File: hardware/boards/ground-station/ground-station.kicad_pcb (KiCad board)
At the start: 4 copper layers, 65 x 59.5 mm, 122 parts, among them J1 USB_A, J101 Raspberry_Pi_2_3, J102 Conn_01x15, J2 Barrel_Jack, J201 U.FL, J202 U.FL, J203 U.FL, J3 Conn_Coaxial, U201 SX1262IMLTRT, U202 RX5808, U203 SW-GPS01, U204 SKY13453-385LF, U3 TPS564242DRLR, U601 ADV7282A-M, U602 AP2127K-1.8, U603 AP2127K-1.8, Y201 32 MHz, Y601 28.63636 MHz

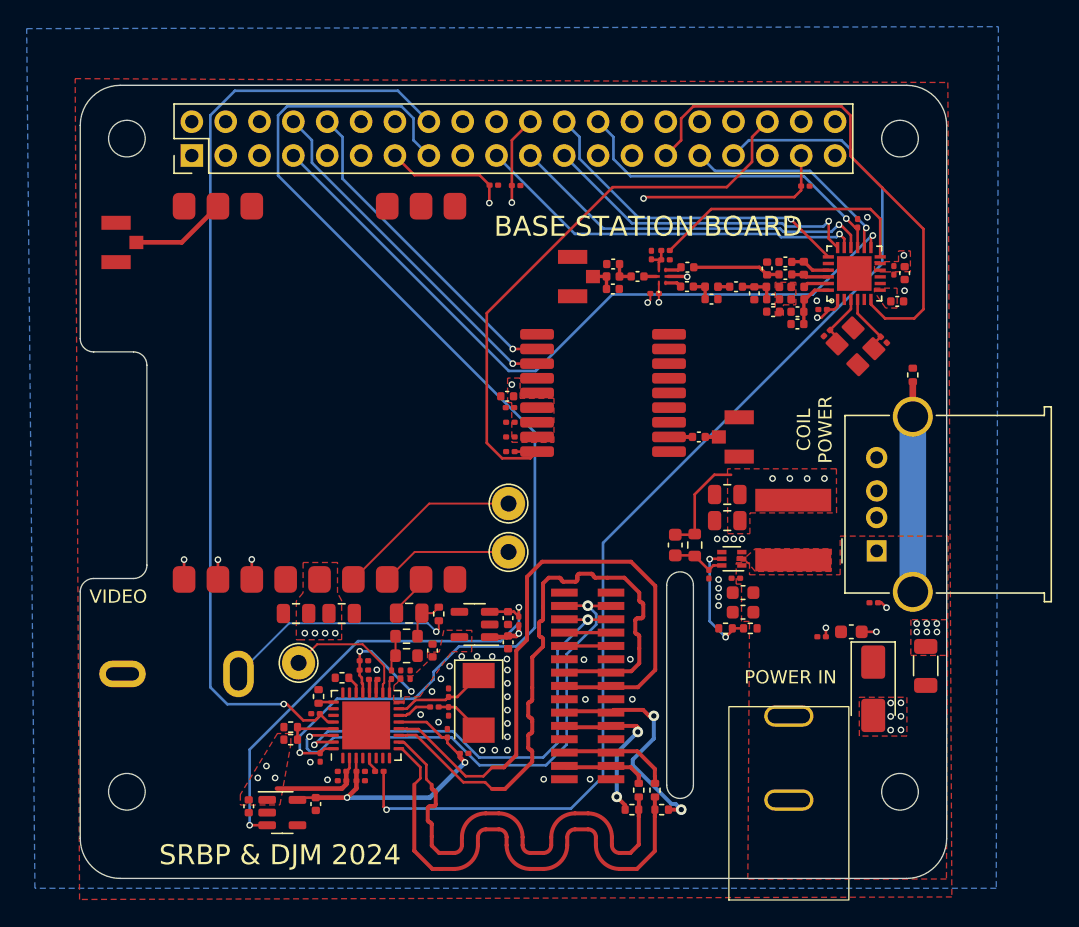
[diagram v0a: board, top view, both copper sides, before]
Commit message: Moved a couple components around and added some ground stitching vias
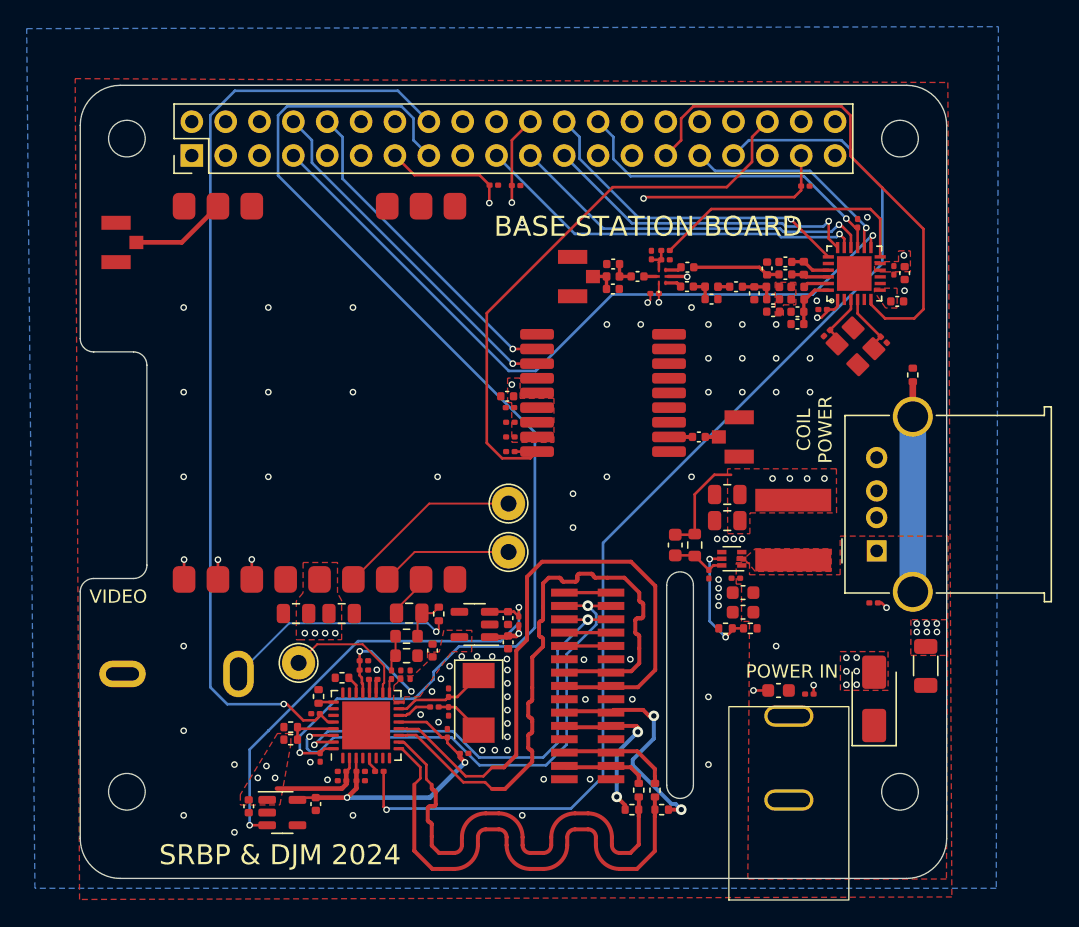
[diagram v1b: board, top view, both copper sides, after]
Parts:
- moved C23 7.02 mm to (152.6, 111.3), turned to 180 degrees
- moved C24 4.40 mm to (154.9, 111.5)
- moved D401 0.76 mm to (159.8, 111.9), turned to 90 degrees
- moved C619 0.70 mm to (121.5, 109.8)
- moved C620 0.70 mm to (121.5, 109.0)
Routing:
- net unconnected-(J102-Pin_15-Pad15): track 0.00 -> 3.50 mm
- net GND: track 4.86 -> 4.87 mm, vias 49 -> 87
